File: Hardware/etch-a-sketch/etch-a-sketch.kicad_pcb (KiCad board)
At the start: 4 copper layers, 100 x 62 mm, 37 parts, among them J1 USART, J2 Conn_02x05_Odd_Even, J3 OLED, J4 Power Connector, SW1 Encoder 1, SW2 Encoder 2, U1 AMS1117-3.3, U2 STM32F401RET6

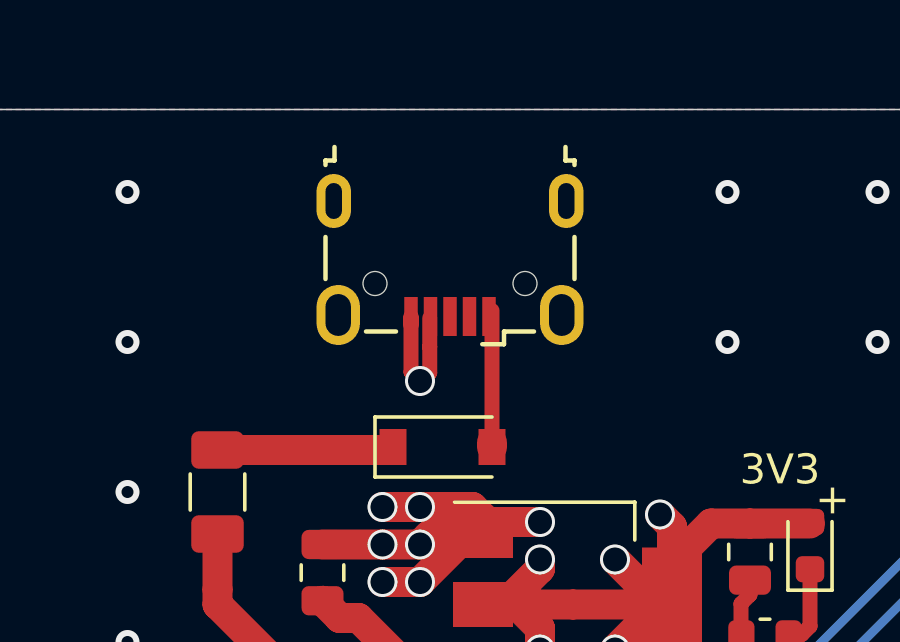
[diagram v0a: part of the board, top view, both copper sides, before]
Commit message: feat: change micro USB footprint to 10118194
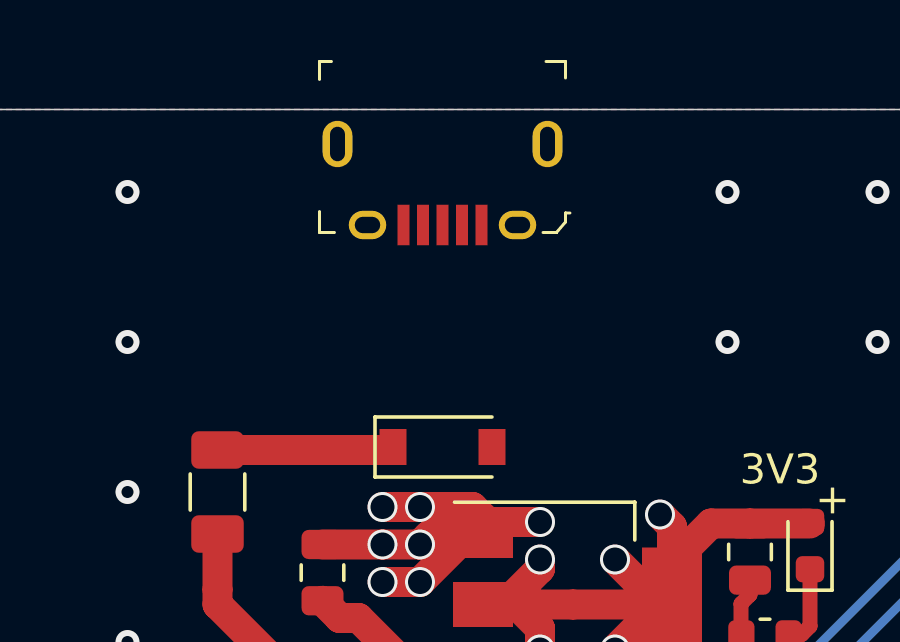
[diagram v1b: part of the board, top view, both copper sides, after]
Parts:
- J4: value Power Connector -> Micro USB B; footprint Connector_USB:USB_Micro-B_Wuerth_629105150521 -> digikey-footprints:USB_Micro_B_Female_10118194-0001LF
- moved J4 1.18 mm to (69.8, 23.9)
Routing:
- net GND: track 74.1 -> 69.3 mm, vias 150 -> 149
- net VCC: track 4.70 -> 0.00 mm

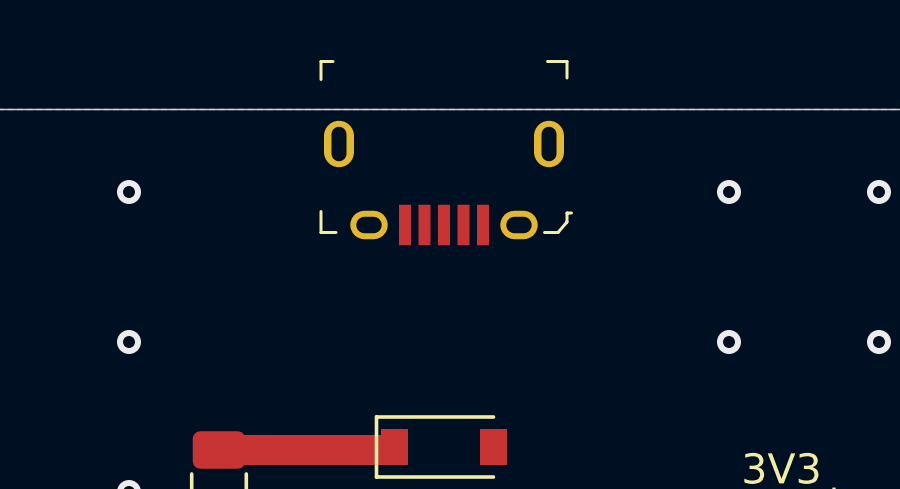
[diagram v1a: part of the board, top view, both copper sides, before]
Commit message: feat: adjust connector position according to datasheet
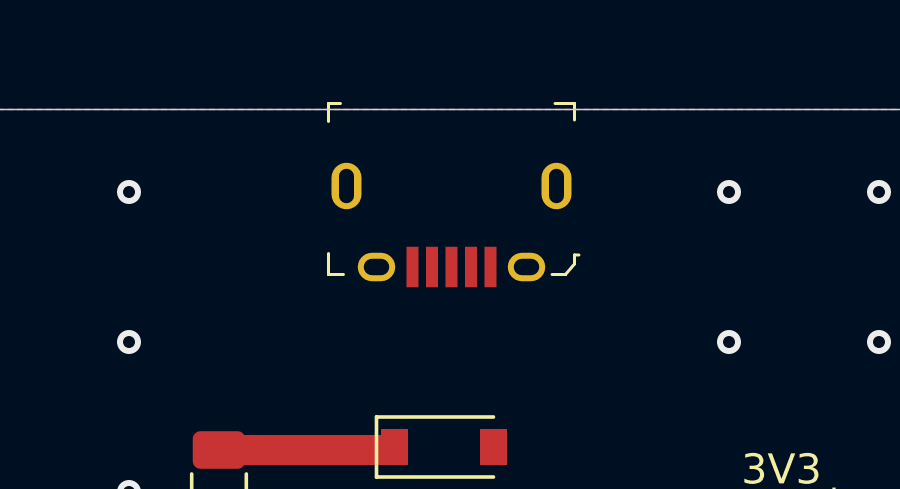
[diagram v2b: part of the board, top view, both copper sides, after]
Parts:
- moved J4 1.42 mm to (70.0, 25.2)
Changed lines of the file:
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@@
   )
   (module digikey-footprints:USB_Micro_B_Female_10118194-0001LF (layer F.Cu)
-    (at 69.75 23.85 180)
+    (at 70 25.25 180)
     (descr http://portal.fciconnect.com/Comergent//fci/drawing/10118194.pdf)
     (attr smd)

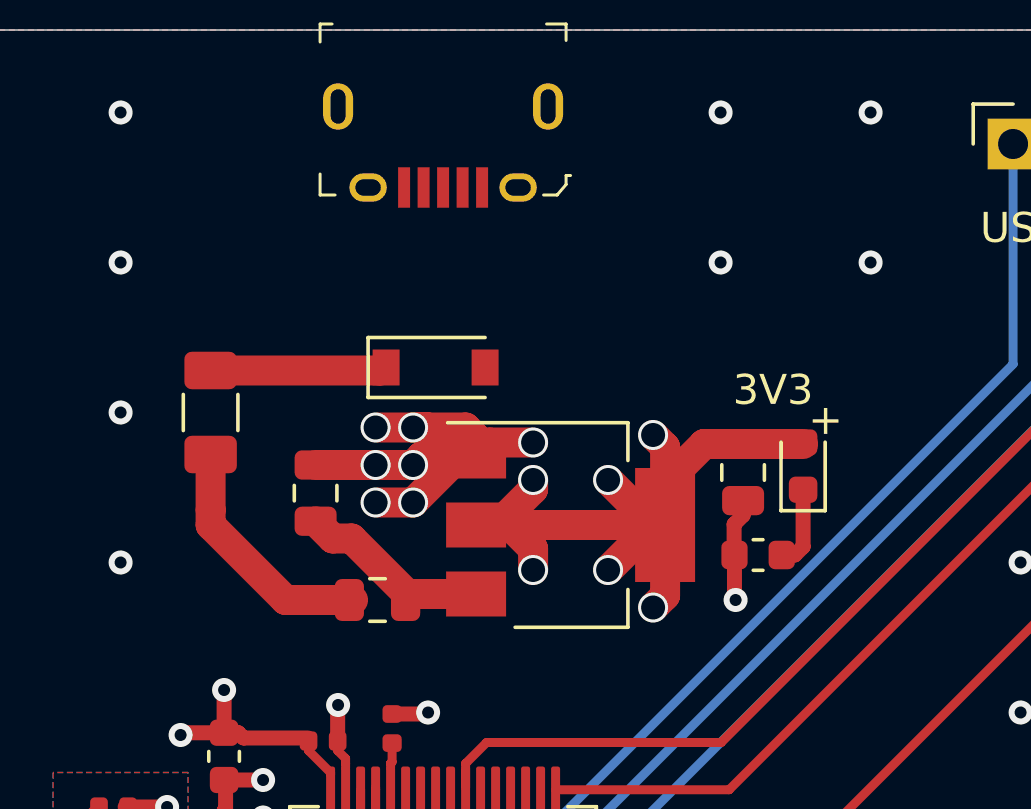
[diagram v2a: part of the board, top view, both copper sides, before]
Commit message: feat: route connector pins
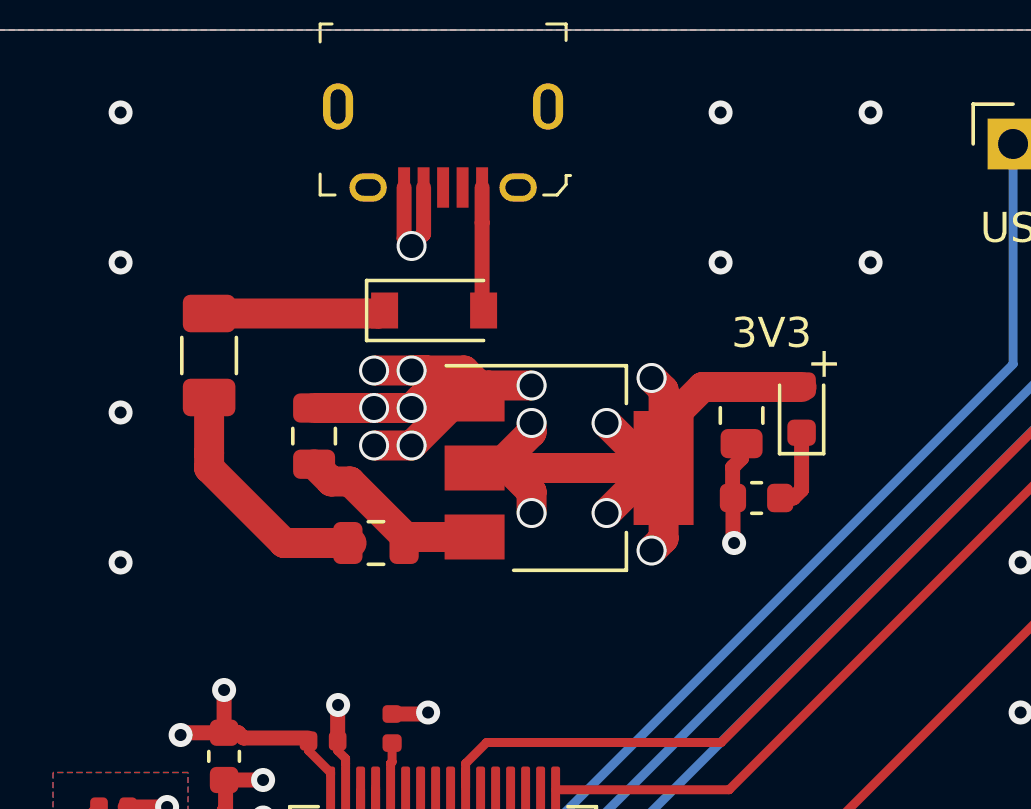
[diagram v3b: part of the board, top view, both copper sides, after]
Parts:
- moved C1 1.90 mm to (65.7, 33.5)
- moved C2 1.90 mm to (80.0, 32.9)
- moved D1 1.90 mm to (69.7, 29.4)
- moved D2 1.90 mm to (82.0, 32.6)
- moved F1 1.90 mm to (62.2, 30.9)
- moved FB1 1.90 mm to (67.8, 37.1)
- moved R1 1.90 mm to (80.5, 35.6)
- moved U1 1.90 mm to (74.2, 34.6)
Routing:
- net GND: track 69.3 -> 73.4 mm, vias 149 -> 150
- net VCC: track 0.00 -> 4.10 mm

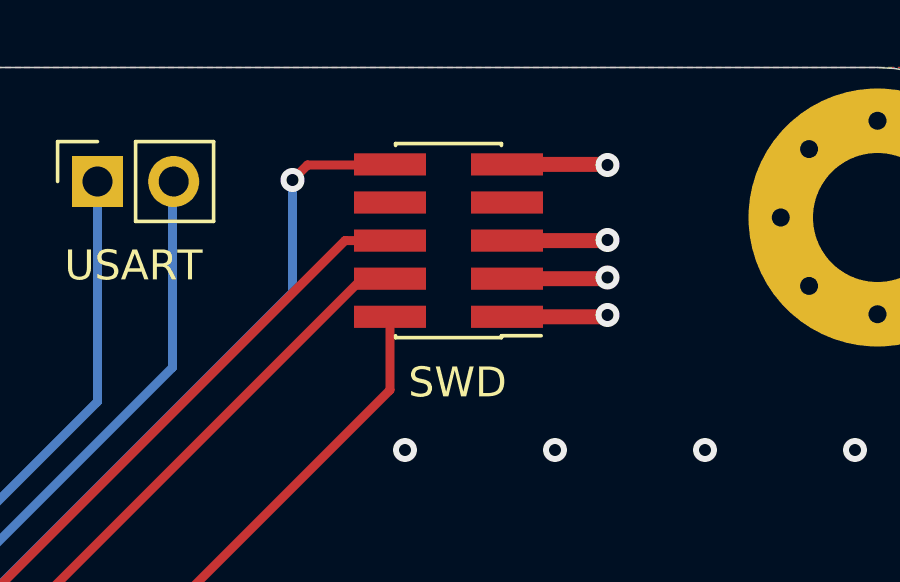
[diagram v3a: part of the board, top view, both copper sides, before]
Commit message: feat: change SWD connector to through-hole
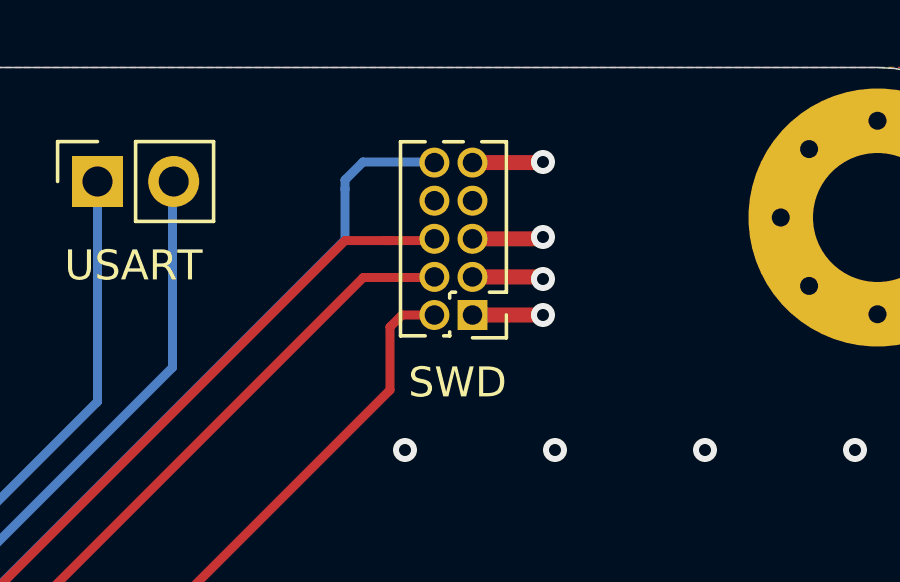
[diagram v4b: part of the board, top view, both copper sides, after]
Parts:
- J2: footprint Connector_PinHeader_1.27mm:PinHeader_2x05_P1.27mm_Vertical_SMD -> Connector_PinHeader_1.27mm:PinHeader_2x05_P1.27mm_Vertical
- moved J2 2.61 mm to (101.5, 28.2)
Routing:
- net GND: track 73.4 -> 70.5 mm
- net SWO: track 36.5 -> 38.2 mm
- net NRST: track 46.9 -> 48.5 mm, vias 2 -> 1
- net SWCLK: track 32.6 -> 34.1 mm
- net SWDIO: track 32.6 -> 34.1 mm
- net +3V3: track 53.6 -> 52.5 mm
